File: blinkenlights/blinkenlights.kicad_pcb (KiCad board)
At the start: 4 copper layers, 160 x 100 mm, 91 parts, among them J201 Conn_03x32_Row_Letter_First, J301 Conn_01x01_Female, J302 Conn_01x01_Female, J303 Conn_01x01_Female, U101 ATF22V10C, U301 AP62250Z6, U302 AP62250Z6

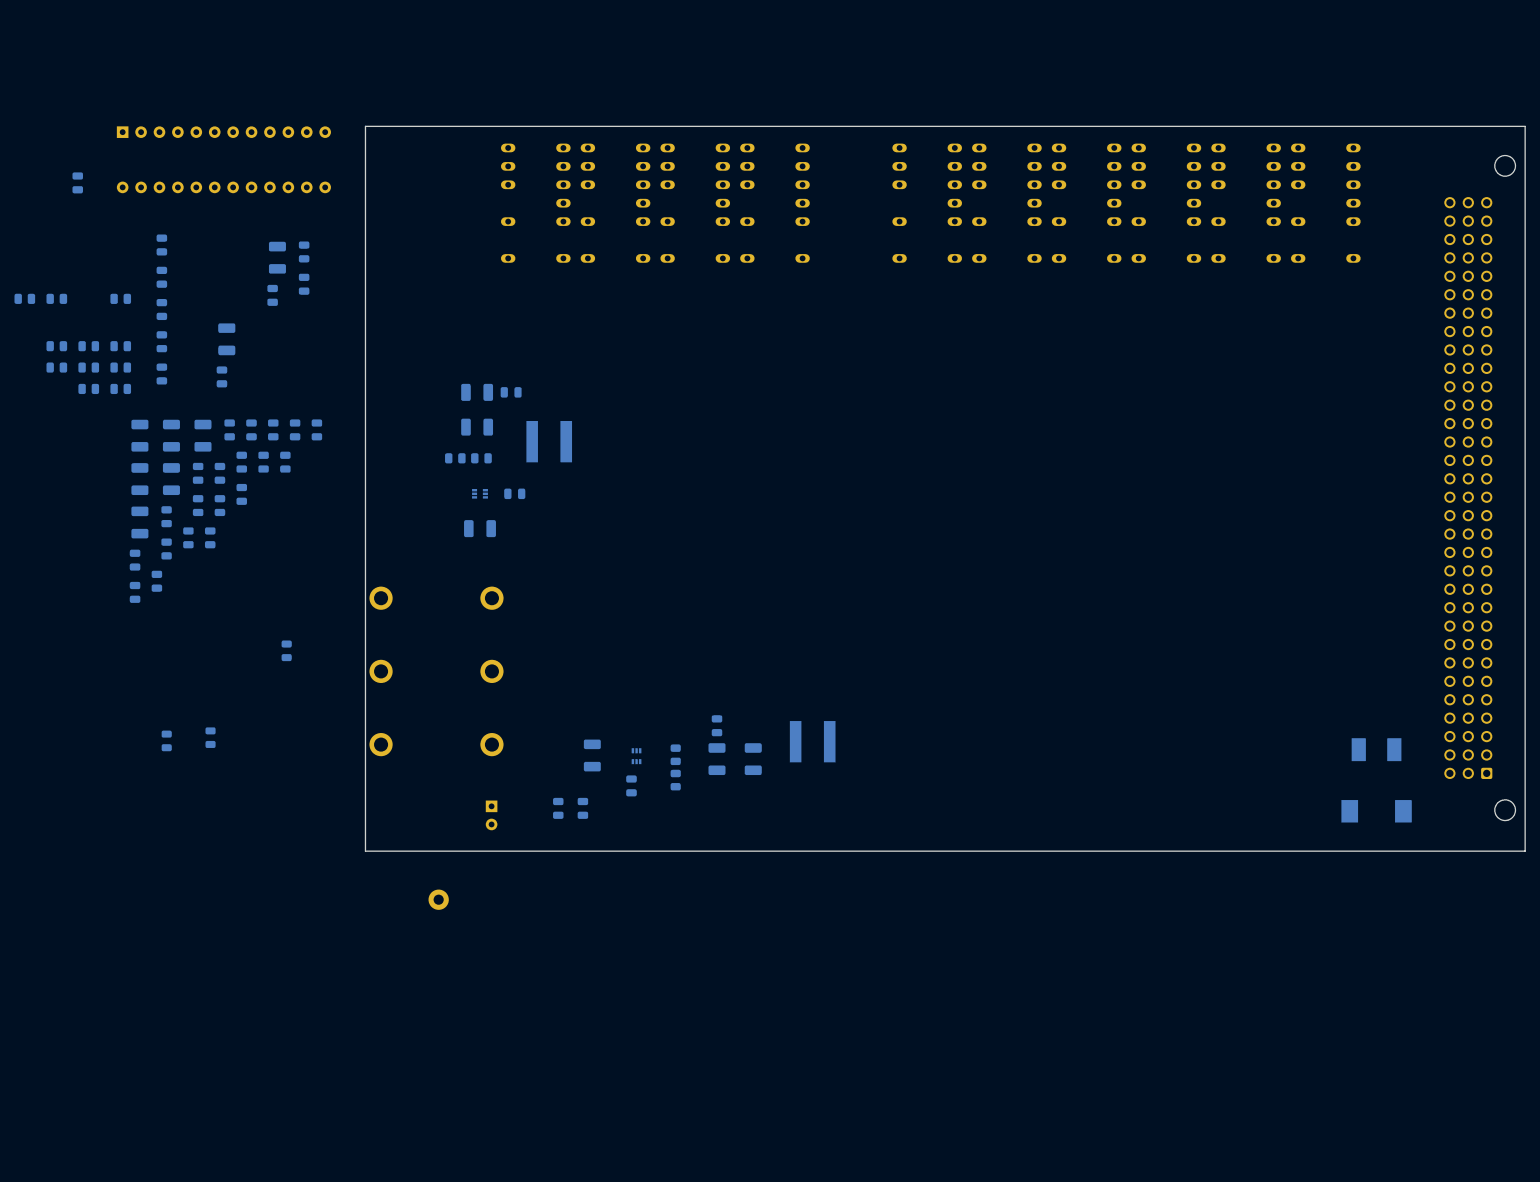
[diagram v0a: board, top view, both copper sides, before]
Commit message: Added ROM sockets to blinkenlights
- Also started routing some of the IOs and powers for the displays
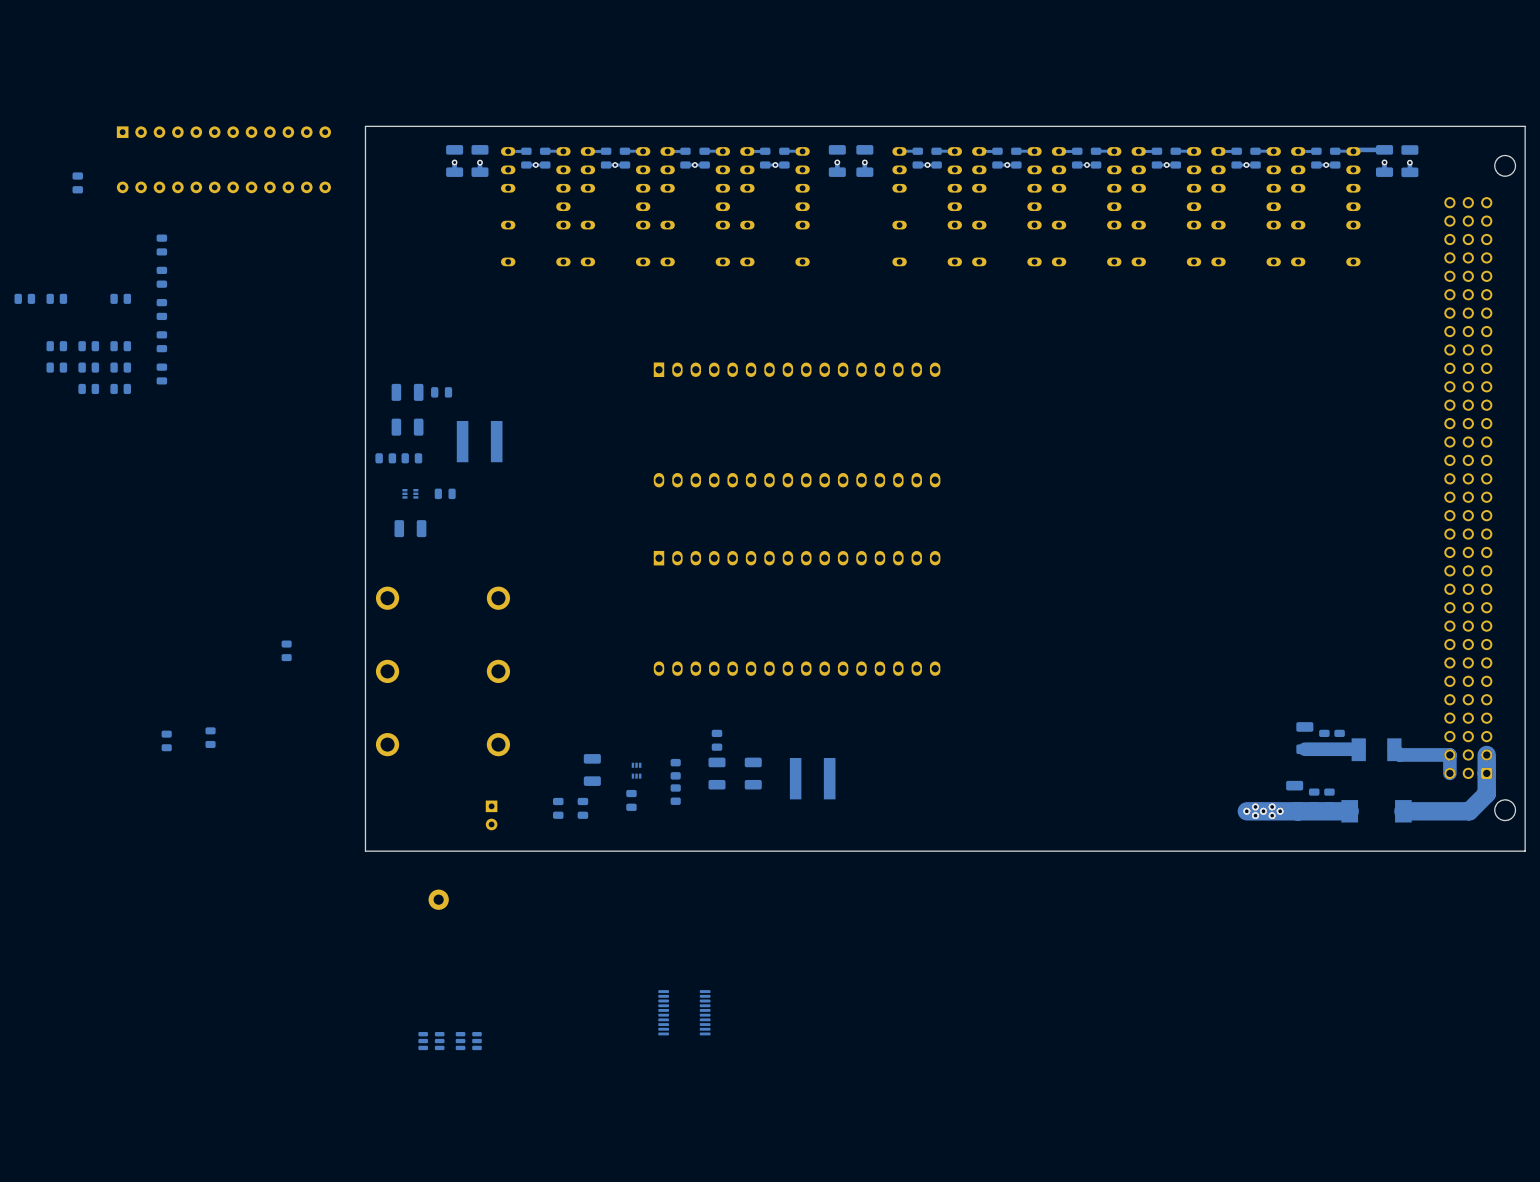
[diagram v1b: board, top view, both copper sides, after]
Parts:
- added U102: SST39SF020, Socket:DIP_Socket-32_W11.9_W12.7_W15.24_W17.78_W18.5_3M_232-1285-00-0602J, B.Cu at (60.5, 53.6)
- added U103: SST39SF020, Socket:DIP_Socket-32_W11.9_W12.7_W15.24_W17.78_W18.5_3M_232-1285-00-0602J, B.Cu at (60.5, 79.6)
- added U104: 74AUC2G07, Package_TO_SOT_SMD:SOT-23-6, B.Cu at (29.1, 146.2)
- added U105: 74AUC2G07, Package_TO_SOT_SMD:SOT-23-6, B.Cu at (34.2, 146.2)
- added U401: 74HC244, Package_SO:TSSOP-20_4.4x6.5mm_P0.65mm, B.Cu at (64.0, 142.3)
- moved C401 180.6 mm to (164.1, 24.8)
- moved C404 171.6 mm to (160.6, 24.8)
- moved C202 161.6 mm to (150.9, 112.8), turned to 90 degrees
- moved C203 160.3 mm to (153.0, 112.8), turned to 90 degrees
- moved C201 160.3 mm to (148.2, 112.5), turned to 90 degrees
- moved C206 159.5 mm to (154.4, 104.7), turned to 90 degrees
- moved C204 156.5 mm to (149.6, 104.4), turned to 90 degrees
- moved C205 154.2 mm to (152.3, 104.7), turned to 90 degrees
- moved C408 152.2 mm to (142.8, 24.4)
- moved C411 146.0 mm to (131.8, 24.4)
- moved C406 145.8 mm to (151.2, 24.4)
- moved C413 145.5 mm to (120.8, 24.4)
- moved C405 145.4 mm to (153.8, 24.4)
- moved C409 140.7 mm to (140.2, 24.4)
- moved C412 134.5 mm to (129.2, 24.4)
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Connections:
- net /D{0..15} renamed /Backplane Connector/D1
- F201 pad 1: +5V -> Net-(F201-Pad1)
- F201 pad 2: Net-(F201-Pad2) -> +5V
- F202 pad 1: +12V -> Net-(F202-Pad1)
- F202 pad 2: Net-(F202-Pad2) -> +12V
- J201 pad a1: Net-(F201-Pad2) -> Net-(F201-Pad1)
- J201 pad a2: Net-(F201-Pad2) -> Net-(F201-Pad1)
- J201 pad c1: Net-(F202-Pad2) -> Net-(F202-Pad1)
- J201 pad c2: Net-(F202-Pad2) -> Net-(F202-Pad1)
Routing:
- net +5V: track 0.00 -> 39.6 mm, vias 0 -> 7
- net GND: track 0.00 -> 33.9 mm, vias 0 -> 16
- net +5VA: track 0.00 -> 29.6 mm
- net Net-(F201-Pad1): track 0.00 -> 17.9 mm
- net Net-(F202-Pad1): track 0.00 -> 10.5 mm
- net +12V: track 0.00 -> 7.47 mm
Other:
- board text added: "High"
- board text added: "Low"

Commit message: Reworked blinkenlights board
- The connector for the CPU board is a female vertical DIN connector
  instead now, which will be a lot less fucky

- Some more LEDs and buttons
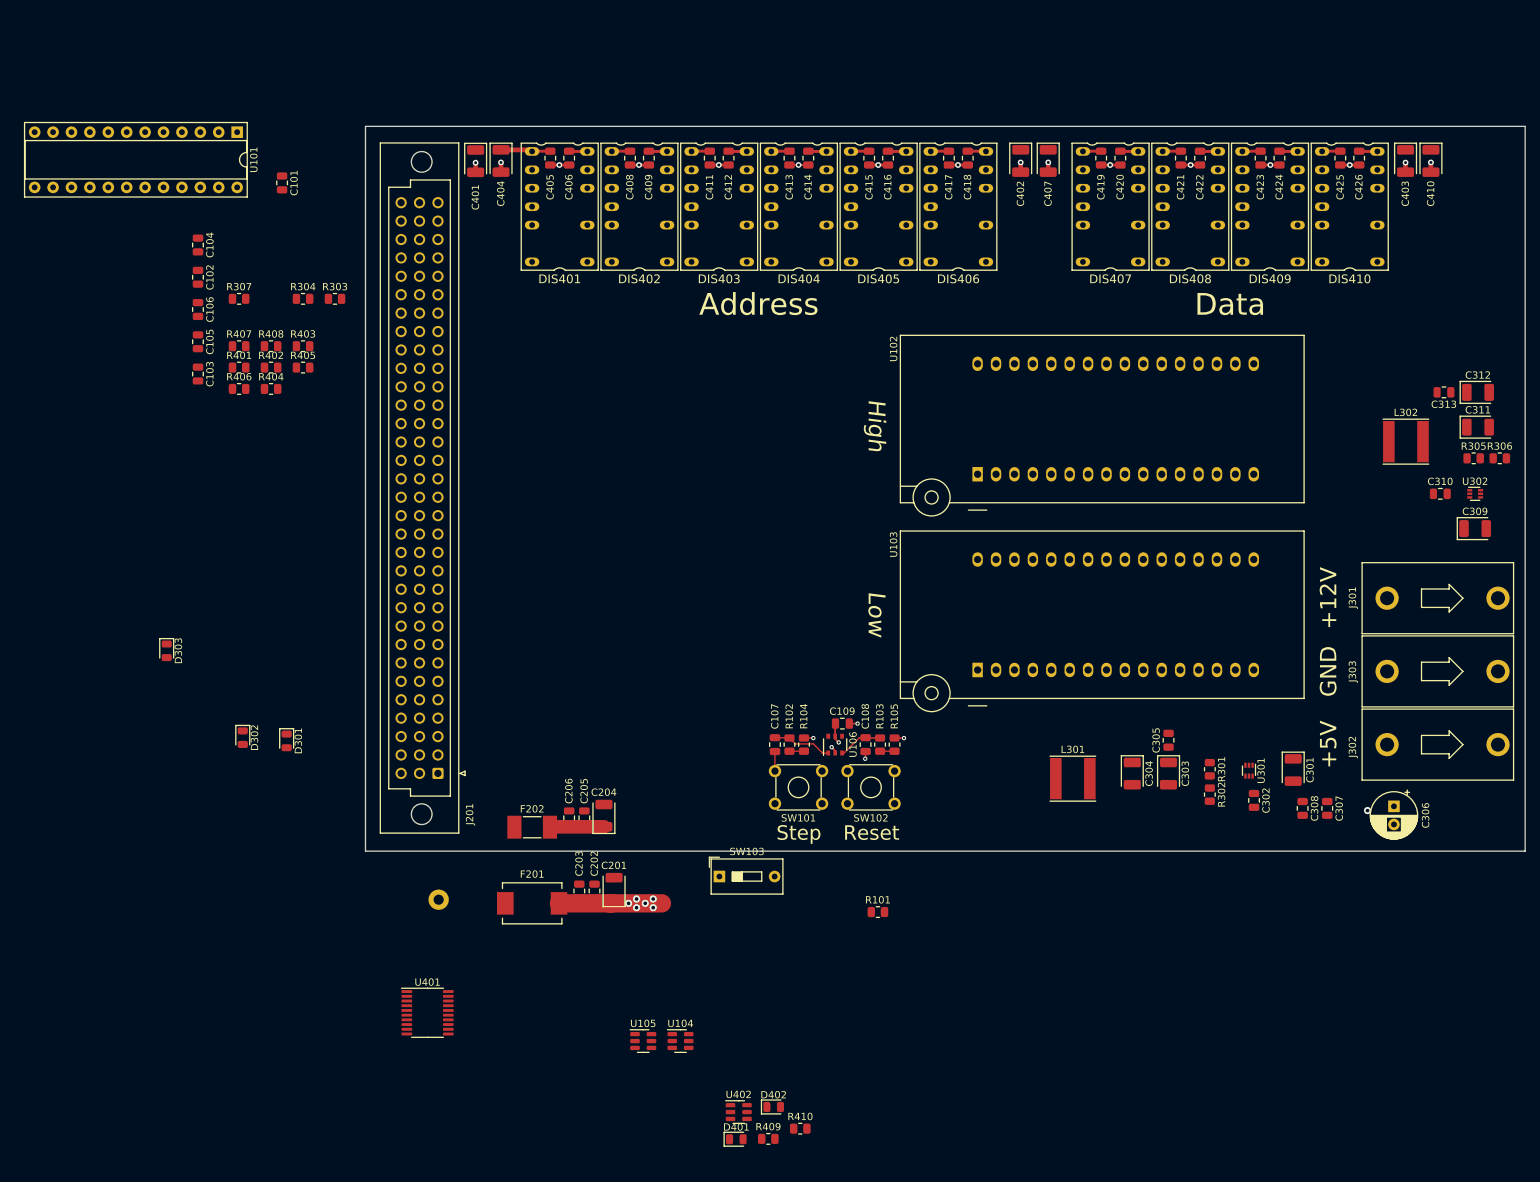
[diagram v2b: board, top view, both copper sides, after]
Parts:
- added C107: 10µF, Capacitor_SMD:C_0805_2012Metric, F.Cu at (76.5, 105.3)
- added C108: 10µF, Capacitor_SMD:C_0805_2012Metric, F.Cu at (89.0, 105.3)
- added C109: 100nF, Capacitor_SMD:C_0805_2012Metric, F.Cu at (85.8, 102.4)
- added D401: Yellow, LED_SMD:LED_0805_2012Metric, F.Cu at (71.2, 159.7)
- added D402: Yellow, LED_SMD:LED_0805_2012Metric, F.Cu at (76.3, 155.3)
- added R101: 10k, Resistor_SMD:R_0805_2012Metric, F.Cu at (90.7, 128.4)
- added R102: 100R, Resistor_SMD:R_0805_2012Metric, F.Cu at (78.5, 105.3)
- added R103: 100R, Resistor_SMD:R_0805_2012Metric, F.Cu at (91.0, 105.3)
- added R104: 10k, Resistor_SMD:R_0805_2012Metric, F.Cu at (80.5, 105.3)
- added R105: 10k, Resistor_SMD:R_0805_2012Metric, F.Cu at (93.0, 105.3)
- added R409: 1k, Resistor_SMD:R_0805_2012Metric, F.Cu at (75.6, 159.7)
- added R410: 1k, Resistor_SMD:R_0805_2012Metric, F.Cu at (80.0, 158.3)
- added SW101: Black, Button_Switch_THT:SW_TH_Tactile_Omron_B3F-10xx, F.Cu at (76.5, 109.0)
- added SW102: Orang, Button_Switch_THT:SW_TH_Tactile_Omron_B3F-10xx, F.Cu at (86.5, 109.0)
- added SW103: SW_DIP_x01, Button_Switch_THT:SW_DIP_SPSTx01_Slide_9.78x4.72mm_W7.62mm_P2.54mm, F.Cu at (68.8, 123.5)
- added U106: 74HC2G14, Package_SO:TSOP-6_1.65x3.05mm_P0.95mm, F.Cu at (84.8, 105.3)
- added U402: 74AUC2G34, Package_TO_SOT_SMD:SOT-23-6, F.Cu at (71.5, 156.0)
- C101, C102, C103, C104, C105, C106, C201, C202, C203, C204, C205, C206, C301, C302, C303, C304, C305, C306, C307, C308, C309, C310, C311, C312, C313, C401, C402, C403, C404, C405, C406, C407, C408, C409, C410, C411, C412, C413, C414, C415, C416, C417, C418, C419, C420, C421, C422, C423, C424, C425, C426, D301, D302, D303, DIS401, DIS402, DIS403, DIS404, DIS405, DIS406, DIS407, DIS408, DIS409, DIS410, F201, F202, J301, J302, J303, L301, L302, R301, R302, R303, R304, R305, R306, R307, R401, R402, R403, R404, R405, R406, R407, R408, U101, U102, U103, U104, U105, U301, U302, U401: moved to F.Cu
- J201: footprint Connector_DIN:DIN41612_R_3x32_Male_Horizontal_THT -> Connector_DIN:DIN41612_C_3x32_Female_Vertical_THT; moved to F.Cu
- moved J301 157.5 mm to (178.4, 85.1)
- moved J302 157.5 mm to (178.4, 105.3)
- moved J303 157.5 mm to (178.4, 95.2)
- moved R306 153.7 mm to (176.5, 65.8), turned to 0 degrees
- moved C311 147.7 mm to (173.5, 61.5), turned to 0 degrees
- moved C312 147.7 mm to (173.5, 56.7), turned to 0 degrees
- moved C309 146.9 mm to (173.1, 75.5), turned to 0 degrees
- moved U302 146.9 mm to (173.1, 70.7), turned to 0 degrees
- moved R305 146.5 mm to (172.9, 65.8), turned to 0 degrees
- moved J201 144.7 mm to (30.0, 109.3), turned to 180 degrees
- moved C313 138.3 mm to (168.8, 56.7), turned to 180 degrees
- moved C310 137.3 mm to (168.3, 70.7), turned to 0 degrees
- moved C410 134.7 mm to (167.0, 24.8)
- moved C401 128.9 mm to (35.2, 24.8)
- moved L302 127.8 mm to (163.6, 63.5), turned to 0 degrees
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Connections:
- U101 pad 10: /A23 -> unconnected-(U101-Pad10)
- U101 pad 11: unconnected-(U101-Pad11) -> /~{POR}
- U101 pad 13: unconnected-(U101-Pad13) -> /~{RUN}
- U101 pad 20: unconnected-(U101-Pad20) -> /RESET
- U101 pad 21: unconnected-(U101-Pad21) -> /HALT
- U101 pad 6: /A19 -> /A20
- U101 pad 7: /A20 -> /A21
- U101 pad 8: /A21 -> /A22
- U101 pad 9: /A22 -> /A23
- U401 pad 8: unconnected-(U401-Pad8) -> /~{AS}
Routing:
- net Net-(F201-Pad1): track 17.9 -> 0.00 mm
- net Net-(F202-Pad1): track 10.5 -> 0.00 mm
- net Net-(C107-Pad1): track 0.00 -> 8.22 mm
- net Net-(C108-Pad1): track 0.00 -> 6.14 mm
- net GND: track 33.9 -> 40.0 mm, vias 16 -> 19
- net +5V: track 39.6 -> 45.1 mm, vias 7 -> 10
- net Net-(R103-Pad1): track 0.00 -> 2.00 mm
- net Net-(R102-Pad1): track 0.00 -> 2.00 mm
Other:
- board text added: "Reset"
- board text added: "Step"

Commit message: did some things
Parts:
- moved U402 24.2 mm to (82.4, 134.4)
- moved D401 24.2 mm to (82.1, 138.1)
- moved D402 24.2 mm to (87.2, 133.7)
- moved R409 24.2 mm to (86.5, 138.1)
- moved R410 24.2 mm to (90.9, 136.6)
- moved U401 16.7 mm to (18.0, 129.4)
- moved U104 16.3 mm to (73.1, 133.0)
- moved U105 16.3 mm to (67.9, 133.0)
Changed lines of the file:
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@@
   )
   (footprint "Resistor_SMD:R_0805_2012Metric" (layer "F.Cu")
-    (at 75.58 159.7)
+    (at 86.51 138.055)
     (descr "Resistor SMD 0805 (2012 Metric), square (rectangular) end terminal, IPC_7351 nominal, (Body size source: IPC-SM-782 page 72, https://www.pcb-3d.com/wordpress/wp-content/uploads/ipc-sm-782a_amendment_1_and_2.pdf), generated with kicad-footprint-generator")
     (tags "resistor")
@@
   )
   (footprint "LED_SMD:LED_0805_2012Metric" (layer "F.Cu")
-    (at 76.32 155.295)
+    (at 87.25 133.65)
     (descr "LED SMD 0805 (2012 Metric), square (rectangular) end terminal, IPC_7351 nominal, (Body size source: https://docs.google.com/spreadsheets/d/1BsfQQcO9C6DZCsRaXUlFlo91Tg2WpOkGARC1WS5S8t0/edit?usp=sharing), generated with kicad-footprint-generator")
     (tags "LED")
@@
   )
   (footprint "Package_SO:TSSOP-20_4.4x6.5mm_P0.65mm" (layer "F.Cu")
-    (at 28.566666 142.3)
+    (at 18 129.4)
     (descr "TSSOP, 20 Pin (JEDEC MO-153 Var AC https://www.jedec.org/document_search?search_api_views_fulltext=MO-153), generated with kicad-footprint-generator ipc_gullwing_generator.py")
     (tags "TSSOP SO")
@@
   )
   (footprint "Package_TO_SOT_SMD:SOT-23-6" (layer "F.Cu")
-    (at 63.466666 146.2)
+    (at 73.076666 133.01)
     (descr "SOT, 6 Pin (https://www.jedec.org/sites/default/files/docs/Mo-178c.PDF variant AB), generated with kicad-footprint-generator ipc_gullwing_generator.py")
     (tags "SOT TO_SOT_SMD")
@@
   )
   (footprint "Package_TO_SOT_SMD:SOT-23-6" (layer "F.Cu")
-    (at 71.5 156)
+    (at 82.43 134.355)
     (descr "SOT, 6 Pin (https://www.jedec.org/sites/default/files/docs/Mo-178c.PDF variant AB), generated with kicad-footprint-generator ipc_gullwing_generator.py")
     (tags "SOT TO_SOT_SMD")
@@
       (effects (font (size 1 1) (thickness 0.15)))
     )
-    (fp_text value ".5A" (at 0 2.7 unlocked) (layer "F.Fab")
+    (fp_text value ".5A" (at -4.4 0 90 unlocked) (layer "F.Fab")
       (effects (font (size 1 1) (thickness 0.15)))
     )
@@
   )
   (footprint "LED_SMD:LED_0805_2012Metric" (layer "F.Cu")
-    (at 71.17 159.745)
+    (at 82.1 138.1)
     (descr "LED SMD 0805 (2012 Metric), square (rectangular) end terminal, IPC_7351 nominal, (Body size source: https://docs.google.com/spreadsheets/d/1BsfQQcO9C6DZCsRaXUlFlo91Tg2WpOkGARC1WS5S8t0/edit?usp=sharing), generated with kicad-footprint-generator")
     (tags "LED")
@@
       (effects (font (size 1 1) (thickness 0.15)))
     )
-    (fp_text value "74HC2G14" (at 0 2.5 90) (layer "F.Fab")
+    (fp_text value "74HC2G14" (at 0 2.5 90) (layer "F.Fab") hide
       (effects (font (size 1 1) (thickness 0.15)))
     )
@@
   )
   (footprint "Resistor_SMD:R_0805_2012Metric" (layer "F.Cu")
-    (at 79.99 158.29)
+    (at 90.92 136.645)
     (descr "Resistor SMD 0805 (2012 Metric), square (rectangular) end terminal, IPC_7351 nominal, (Body size source: IPC-SM-782 page 72, https://www.pcb-3d.com/wordpress/wp-content/uploads/ipc-sm-782a_amendment_1_and_2.pdf), generated with kicad-footprint-generator")
     (tags "resistor")
@@
   )
   (footprint "Package_TO_SOT_SMD:SOT-23-6" (layer "F.Cu")
-    (at 58.316666 146.2)
+    (at 67.926666 133.01)
     (descr "SOT, 6 Pin (https://www.jedec.org/sites/default/files/docs/Mo-178c.PDF variant AB), generated with kicad-footprint-generator ipc_gullwing_generator.py")
     (tags "SOT TO_SOT_SMD")
